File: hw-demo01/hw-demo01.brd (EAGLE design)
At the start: 54.3 x 58.4 mm, 24 parts, among them IC3 MCP2562T, IC4 STM32F042, Q1 BTS50010

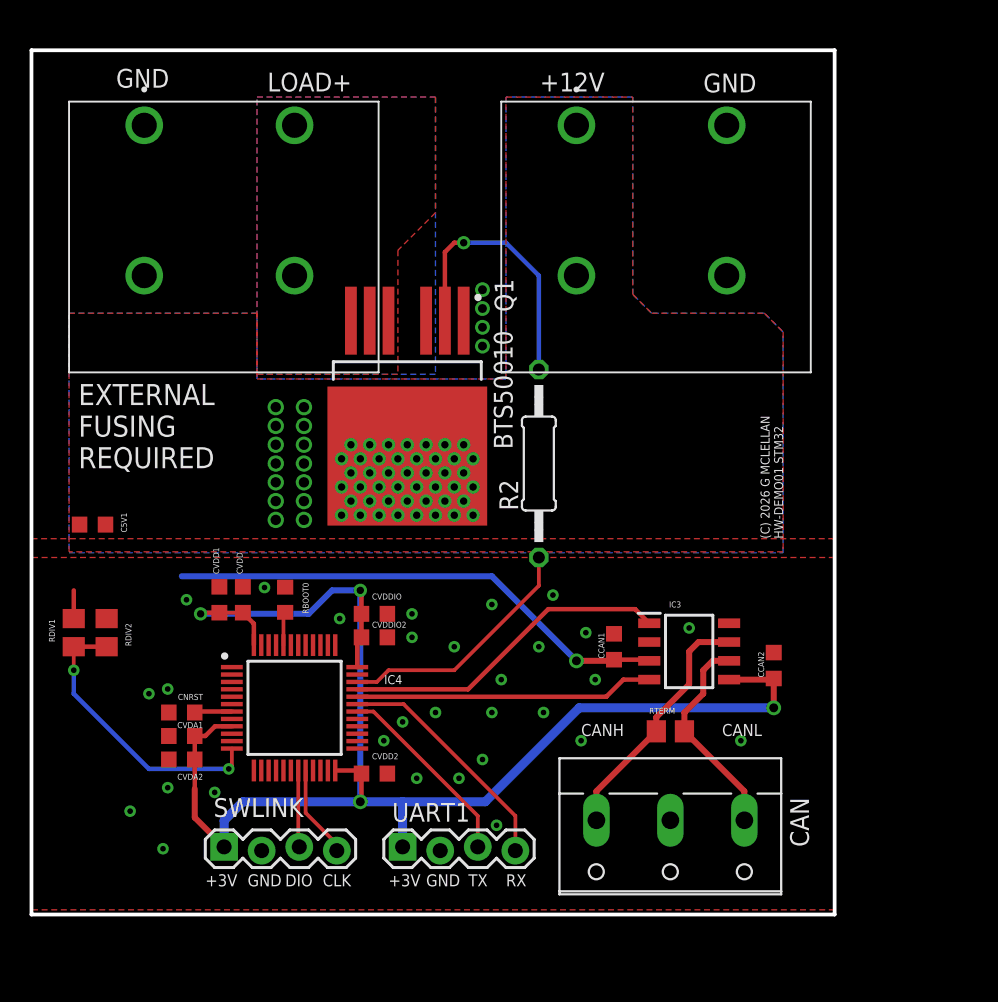
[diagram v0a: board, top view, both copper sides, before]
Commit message: fine tune layout, add voltage regulators
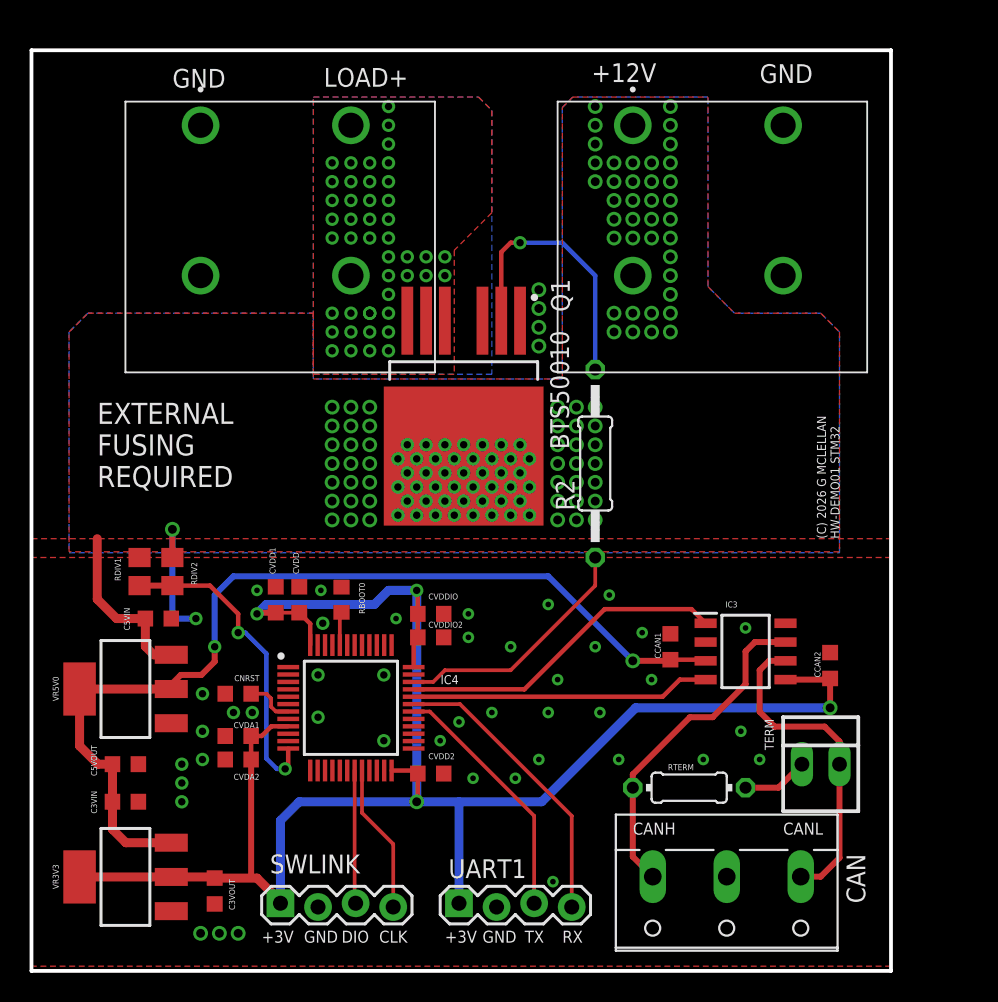
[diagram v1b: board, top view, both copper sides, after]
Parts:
- removed C5V1: 1u, rcl:C0603K
- added C3VIN, C3VOUT, C5VIN, C5VOUT: 1u, rcl:C0603K
- added TERM: 22-23-2021, con-molex:22-23-2021
- added VR3V3, VR5V0: (no value), SparkFun-PowerIC:SOT223
- RTERM: device rcl:R0805 -> rcl:0204/7
- moved RDIV2 6.07 mm to (10.8, 27.0)
- moved RDIV1 6.07 mm to (8.57, 27.0)
- moved SWLINK 5.39 mm to (18.1, 4.45)
- moved UART1 5.39 mm to (30.2, 4.45)
- moved CAN 5.39 mm to (48.3, 5.08)
- moved CNRST 4.02 mm to (15.2, 18.7)
- moved RTERM 4.02 mm to (45.7, 12.4)
- moved +12V 3.81 mm to (47.0, 52.1)
- moved CCAN1 3.81 mm to (44.5, 21.9)
- moved IC3 3.81 mm to (49.5, 21.6)
- moved RBOOT0 3.81 mm to (22.2, 25.1)
- moved CVDA1 3.81 mm to (15.2, 15.9)
- moved CVDA2 3.81 mm to (15.2, 14.3)
- moved CVDD 3.81 mm to (19.4, 25.1)
- moved CVDD1 3.81 mm to (17.8, 25.1)
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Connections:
- removed net N$9: C5V1.2, RDIV2.1
- new net N$1: RTERM.1, TERM.1
- net +12V: now also C5VIN.1, VR5V0.3; no longer C5V1.1
- net +3V3: now also C3VOUT.1, VR3V3.2, VR3V3.4
- net +5V: now also C3VIN.1, C5VOUT.1, VR3V3.3, VR5V0.2, VR5V0.4
- net CANL: now also TERM.2; no longer RTERM.1
- net GND: now also C3VIN.2, C3VOUT.2, C5VIN.2, C5VOUT.2, RDIV2.1, VR3V3.1, VR5V0.1
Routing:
- net +5V: track 34.1 -> 66.1 mm, vias 1 -> 2
- net +3V3: track 101.6 -> 125.4 mm
- net +12V: track 1.91 -> 11.8 mm, vias 59 -> 126
- net GND: track 0.00 -> 9.53 mm, vias 34 -> 48
- net CANL: track 14.4 -> 22.1 mm
- net CANH: track 17.0 -> 22.8 mm
- net N$1: track 0.00 -> 4.47 mm
- net SWCLK: track 6.29 -> 10.1 mm
- net TX1: track 13.2 -> 17.0 mm
- net RX1: track 16.2 -> 20.0 mm
- net SWDIO: track 5.19 -> 9.00 mm
- net ADC2: track 19.4 -> 21.3 mm
- net N$8: track 2.53 -> 3.33 mm
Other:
- board size 54.3 x 58.4 mm -> 58.1 x 62.2 mm

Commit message: Added test points, current monitoring and a few layout refinements
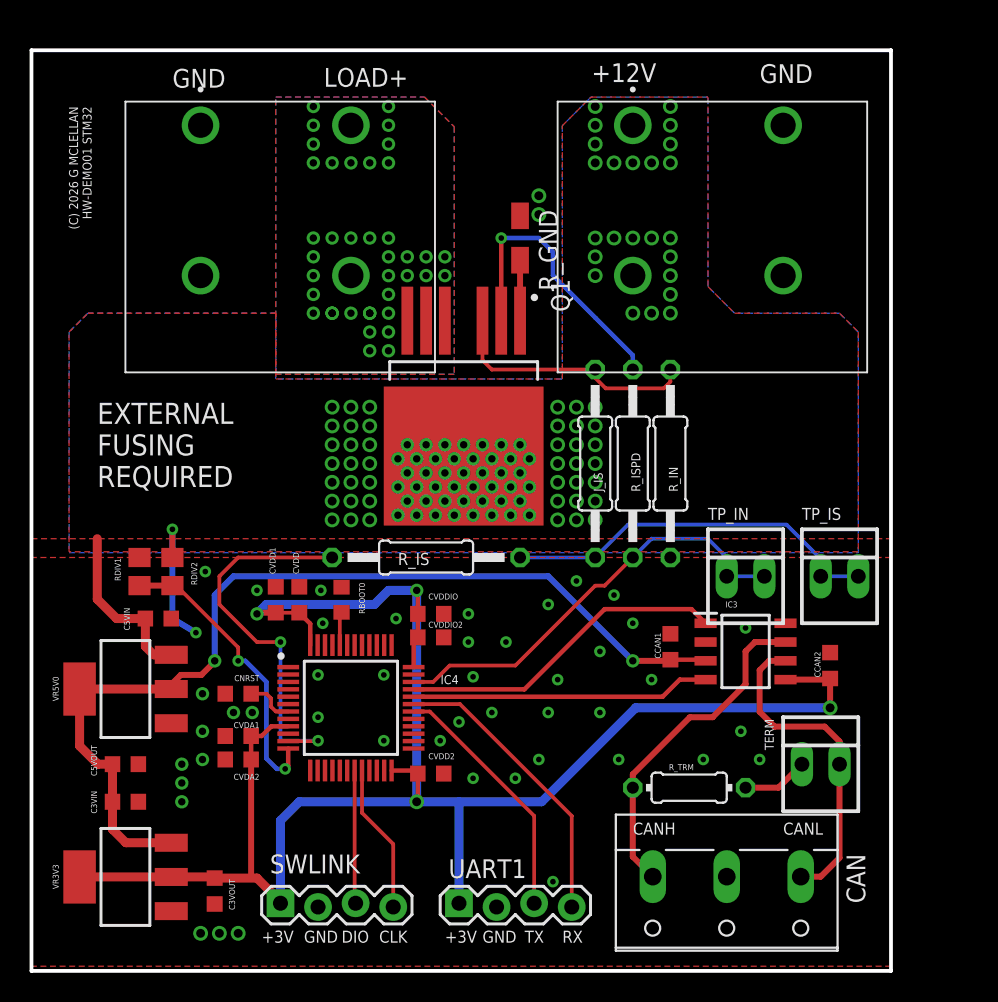
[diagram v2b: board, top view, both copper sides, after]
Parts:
- added R_GND: 0R0, rcl:R1206W
- added R_IN: 4K7, rcl:0207/12
- added R_IS: 10K, rcl:0207/12
- added R_ISPD: 1K0, rcl:0207/12
- added TP_IN, TP_IS: (no value), con-molex:22-23-2021
- J_IS: value 100 -> 0R0
- TERM: value 22-23-2021 -> (none)
- turned J_IS to 270 degrees
- renumbered R2 to J_IS, RTERM to R_TRM
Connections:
- new net ADC1: IC4.11, R_IS.2
- new net IS: J_IS.1, Q1.3, R_ISPD.2
- new net N$2: J_IS.2, R_IS.1, TP_IS.1, TP_IS.2
- new net N$3: Q1.1, R_GND.2
- net CTL3: now also R_IN.1, TP_IN.1, TP_IN.2; no longer J_IS.1
- net CTL3`: now also R_IN.2; no longer J_IS.2
- net GND: now also R_GND.1, R_ISPD.1; no longer Q1.1
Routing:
- net ADC1: track 0.00 -> 26.5 mm, vias 0 -> 2
- net N$2: track 0.00 -> 25.9 mm
- net IS: track 0.00 -> 17.5 mm
- net CTL3: track 16.9 -> 29.5 mm
- net N$3: track 0.00 -> 4.09 mm
- net ADC2: track 21.3 -> 20.0 mm
- net CTL3`: track 18.5 -> 19.6 mm
- net GND: track 9.53 -> 9.79 mm, vias 48 -> 49
- net +12V: vias 126 -> 111

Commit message: Fix some capacitor packages and DRC errors
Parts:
- removed C3VIN: 1u, rcl:C0603K
- added C12VIN: 1u, rcl:C1206K
- C3VOUT, C5VOUT: device rcl:C0603K -> rcl:C0805K
- C5VIN: device rcl:C0603K -> rcl:C1206K
- moved C5VIN 12.6 mm to (7.62, 11.4)
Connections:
- net +12V: now also C12VIN.1; no longer C5VIN.1
- net +5V: now also C5VIN.1; no longer C3VIN.1
- net GND: now also C12VIN.2; no longer C3VIN.2
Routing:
- net +12V: track 11.8 -> 15.0 mm
- net +5V: track 66.1 -> 68.8 mm
- net ADC1: track 26.5 -> 25.9 mm

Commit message: fixed board footprint for smart switch, added recommended Vs capacitor
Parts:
- added C_VS: 100n, rcl:C0603K
- Q1: value BTS50010 -> (none); device BTS50010-1TAD:TO127P1500X450-7_8N-V1 -> BTS500101TADATMA2:BTS500101TADATMA2
- moved Q1 1.90 mm to (30.5, 37.5), turned to 180 degrees
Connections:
- net +12V: now also C_VS.1, Q1.4; no longer Q1.8
- net GND: now also C_VS.2
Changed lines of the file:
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@@
 <attribute name="VALUE" x="48.26" y="13.97" size="0.4064" layer="27" font="vector" ratio="14" rot="R180"/>
-</element>
-<element name="Q1" library="BTS50010-1TAD" package="TO127P1500X450-7_8N-V1" value="BTS50010" x="30.48" y="39.37" smashed="yes" rot="R270">
-<attribute name="NAME" x="36.382" y="46.767" size="1.27" layer="25" font="vector" ratio="14" rot="R270"/>
 </element>
 <element name="R_IN" library="rcl" package="0207/12" value="4K7" x="41.91" y="34.29" smashed="yes" rot="R90">
@@
 <attribute name="NAME" x="26.035" y="27.432" size="0.8128" layer="25" ratio="14"/>
 </element>
+<element name="Q1" library="BTS500101TADATMA2" package="BTS500101TADATMA2" value="" x="30.48" y="37.465" rot="R180">
+<attribute name="MOUSER_PRICE-STOCK" value="https://www.mouser.co.uk/ProductDetail/Infineon-Technologies/BTS500101TADATMA2?qs=l7cgNqFNU1huaQviZWv9NQ%3D%3D" x="30.48" y="37.465" size="1.778" layer="27" rot="R180" display="off"/>
+<attribute name="HEIGHT" value="4.5mm" x="30.48" y="37.465" size="1.778" layer="27" rot="R180" display="off"/>
+<attribute name="DESCRIPTION" value="Power Switch ICs - Power Distribution MULTICHIP PROFET &amp; GD" x="30.48" y="37.465" size="1.778" layer="27" rot="R180" display="off"/>
+<attribute name="MANUFACTURER_NAME" value="Infineon" x="30.48" y="37.465" size="1.778" layer="27" rot="R180" display="off"/>
+<attribute name="MANUFACTURER_PART_NUMBER" value="BTS500101TADATMA2" x="30.48" y="37.465" size="1.778" layer="27" rot="R180" display="off"/>
+<attribute name="MOUSER_PART_NUMBER" value="726-BTS500101TADATM2" x="30.48" y="37.465" size="1.778" layer="27" rot="R180" display="off"/>
+</element>
+<element name="C_VS" library="rcl" package="C0603K" value="100n" x="36.83" y="54.2925" rot="R180"/>
 </elements>
 <signals>
 <signal name="SW3">
-<contactref element="Q1" pad="6"/>
-<contactref element="Q1" pad="5"/>
-<contactref element="Q1" pad="7"/>
 <polygon width="0.4064" layer="1" rank="3">
 <vertex x="17.78" y="59.055"/>
@@
 <via x="20.32" y="57.15" extent="1-16" drill="0.5"/>
 <via x="20.32" y="58.42" extent="1-16" drill="0.5"/>
+<contactref element="Q1" pad="5"/>
+<contactref element="Q1" pad="7"/>
+<contactref element="Q1" pad="6"/>
 </signal>
 <signal name="GND">
@@
 <via x="14.9225" y="17.4625" extent="1-16" drill="0.381"/>
 <via x="16.1925" y="17.4625" extent="1-16" drill="0.381"/>
+<contactref element="C_VS" pad="2"/>
 </signal>
 <signal name="CANH">
@@
 </polygon>
 <contactref element="RDIV1" pad="2"/>
-<contactref element="Q1" pad="8"/>
 <contactref element="+12V" pad="1_2"/>
 <contactref element="+12V" pad="1_1"/>
@@
 <wire x1="8.5725" y1="27.9375" x2="8.5725" y2="27.94" width="0.3048" layer="1"/>
 <wire x1="8.5725" y1="27.94" x2="6.4375" y2="27.94" width="0.3048" layer="1"/>
+<contactref element="Q1" pad="4"/>
+<contactref element="C_VS" pad="1"/>
 </signal>
 <signal name="+5V">
@@
 </signal>
 <signal name="CTL3`">
-<contactref element="Q1" pad="2"/>
 <contactref element="R_IN" pad="2"/>
-<wire x1="33.02" y1="43.945" x2="33.02" y2="49.53" width="0.3048" layer="1"/>
 <via x="33.02" y="49.53" extent="1-16" drill="0.381"/>
 <wire x1="36.5125" y1="47.007584375" x2="36.5125" y2="48.5775" width="0.3048" layer="16"/>
@@
 <wire x1="35.56" y1="49.53" x2="33.02" y2="49.53" width="0.3048" layer="16"/>
 <wire x1="41.91" y1="40.64" x2="41.91" y2="41.610084375" width="0.3048" layer="16"/>
-<wire x1="41.91" y1="41.610084375" x2="39.387584375" y2="44.1325" width="0.3048" layer="16"/>
-<wire x1="39.387584375" y1="44.1325" x2="36.5125" y2="47.007584375" width="0.3048" layer="16"/>
+<wire x1="41.91" y1="41.610084375" x2="36.5125" y2="47.007584375" width="0.3048" layer="16"/>
+<contactref element="Q1" pad="2"/>
+<wire x1="33.02" y1="49.53" x2="33.02" y2="43.89" width="0.4064" layer="1"/>
 </signal>
 <signal name="N$1">
@@
 </signal>
 <signal name="IS">
-<contactref element="Q1" pad="3"/>
 <contactref element="R_ISPD" pad="2"/>
 <contactref element="J_IS" pad="1"/>
-<wire x1="31.75" y1="43.945" x2="31.75" y2="41.275" width="0.254" layer="1"/>
-<wire x1="31.75" y1="41.275" x2="32.385" y2="40.64" width="0.254" layer="1"/>
-<wire x1="32.385" y1="40.64" x2="39.37" y2="40.64" width="0.254" layer="1"/>
+<wire x1="39.37" y1="40.64" x2="32.385" y2="40.64" width="0.254" layer="1"/>
+<wire x1="32.385" y1="40.64" x2="31.75" y2="41.275" width="0.254" layer="1"/>
+<wire x1="31.75" y1="41.275" x2="31.75" y2="43.89" width="0.254" layer="1"/>
 <wire x1="39.37" y1="40.64" x2="39.37" y2="40.07995" width="0.254" layer="1"/>
 <wire x1="39.37" y1="40.07995" x2="40.07995" y2="39.37" width="0.254" layer="1"/>
@@
 <wire x1="44.0009875" y1="39.37" x2="44.45" y2="39.8190125" width="0.254" layer="1"/>
 <wire x1="44.45" y1="39.8190125" x2="44.45" y2="40.64" width="0.254" layer="1"/>
+<contactref element="Q1" pad="3"/>
 </signal>
 <signal name="ADC1">
@@
 <wire x1="18.0975" y1="22.225" x2="16.51" y2="22.225" width="0.254" layer="1"/>
 </signal>
-<signal name="N$3">
-<contactref element="Q1" pad="1"/>
-<contactref element="R_GND" pad="2"/>
-<wire x1="34.29" y1="43.945" x2="34.29" y2="48.031" width="0.4064" layer="1"/>
-</signal>
 <signal name="N$2">
 <contactref element="TP_IS" pad="2"/>
@@
 <wire x1="54.61" y1="26.67" x2="57.15" y2="26.67" width="0.254" layer="16"/>
 </signal>
+<signal name="N$3">
+<contactref element="Q1" pad="1"/>
+<contactref element="R_GND" pad="2"/>
+<wire x1="34.29" y1="43.89" x2="34.29" y2="48.031" width="0.4064" layer="1"/>
+</signal>
 </signals>

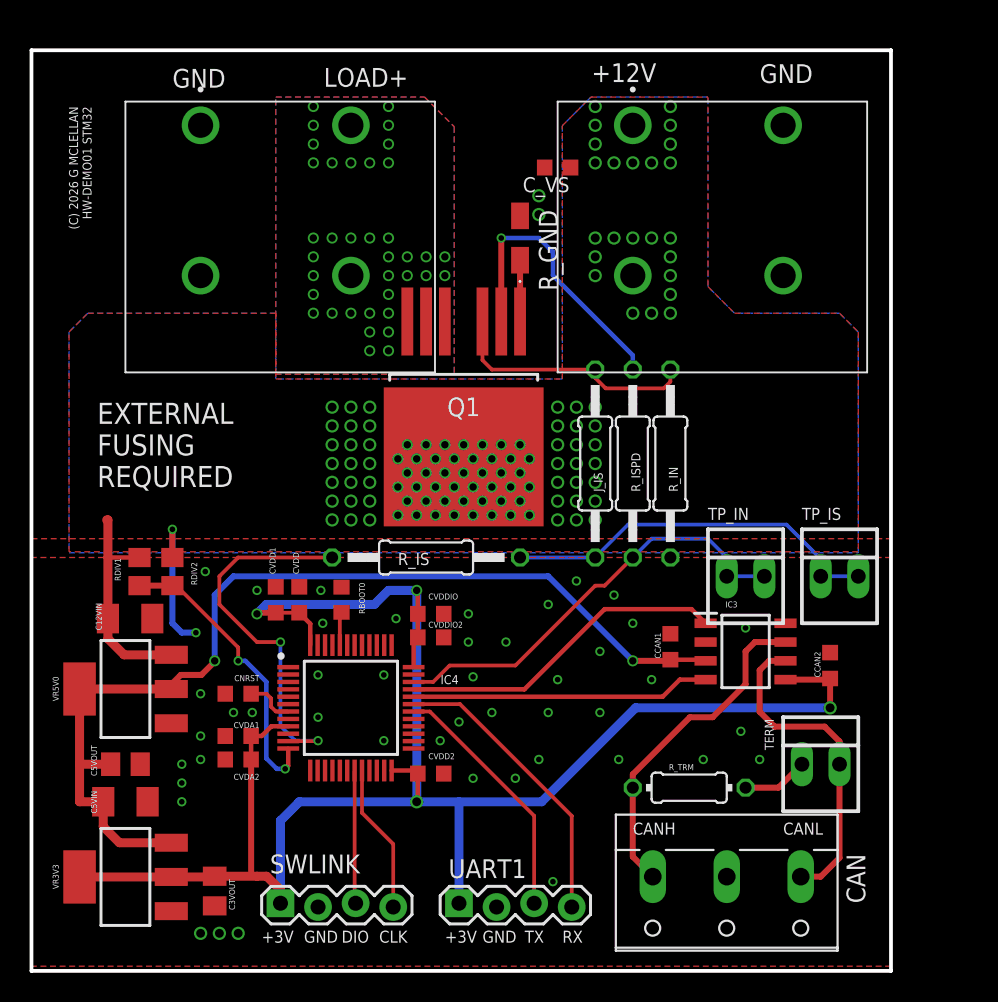
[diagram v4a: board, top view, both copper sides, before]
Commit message: adjusted board dimensions to eliminate connector overlap
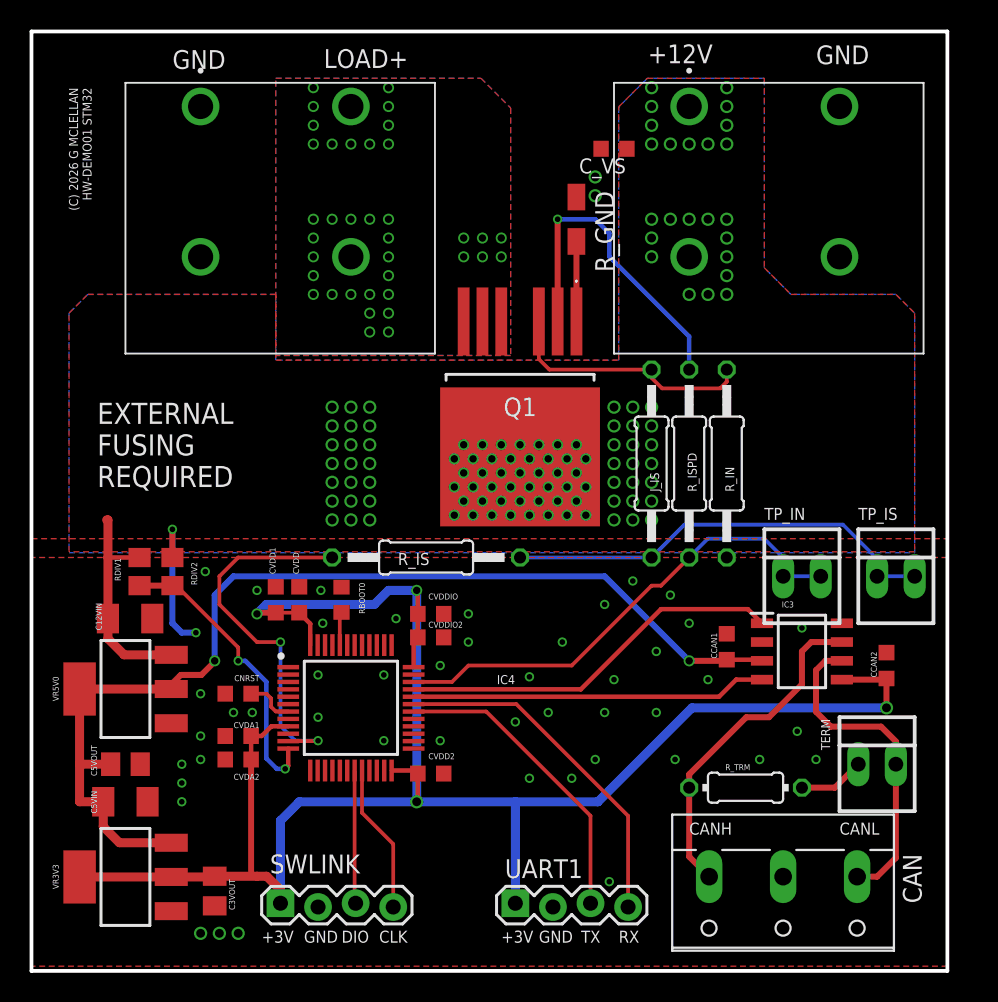
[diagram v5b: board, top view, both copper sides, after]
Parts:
- moved C_VS 4.02 mm to (40.6, 55.6)
- moved R_GND 4.02 mm to (38.1, 50.8)
- moved +12V 4.02 mm to (50.8, 53.3)
- moved CAN 3.81 mm to (52.1, 5.08)
- moved CCAN2 3.81 mm to (59.1, 20.6)
- moved IC3 3.81 mm to (53.3, 21.6)
- moved J_IS 3.81 mm to (43.2, 34.3)
- moved R_IN 3.81 mm to (45.7, 34.3)
- moved R_TRM 3.81 mm to (49.5, 12.4)
- moved TERM 3.81 mm to (58.4, 14.0)
- moved TP_IN 3.81 mm to (53.3, 26.7)
- moved Q1 3.81 mm to (34.3, 37.5)
- moved CCAN1 3.81 mm to (48.3, 21.9)
- moved R_ISPD 3.81 mm to (48.3, 34.3)
- moved TP_IS 3.81 mm to (59.7, 26.7)
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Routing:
- net RX1: track 20.0 -> 23.8 mm
- net CTL3: track 29.5 -> 33.3 mm
- net CAN_TX: track 22.4 -> 26.2 mm
- net CAN_RX: track 20.2 -> 24.0 mm
- net +5V: track 68.8 -> 72.6 mm
- net +3V3: track 125.8 -> 129.6 mm
- net TX1: track 17.0 -> 20.8 mm
- net N$2: track 25.9 -> 29.7 mm
- net CTL3`: track 19.7 -> 22.2 mm
- net N$3: track 4.14 -> 5.41 mm
- net GND: vias 49 -> 50
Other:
- board size 58.1 x 62.2 mm -> 61.9 x 63.5 mm
